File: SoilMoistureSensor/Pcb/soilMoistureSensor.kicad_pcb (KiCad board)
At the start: 2 copper layers, 93 parts, among them J1 USB_B_Micro, J2 Conn_01x03, J3 Conn_01x02, J4 Conn_01x03, J5 Conn_01x03, J6 Conn_01x01, J7 Conn_01x01, J8 Conn_01x01, J9 Conn_01x01, U1 W25Q16JVUXIQ, U10 74AUC2G66, U11 TLV9002S, U12 MCP4011-xxxxMS, U2 RP2040, U3 AP63357Q, U4 74AUC2G86, U5 MIC5504-2.5YM5, U6 74AUC2G86, U7 74AUC2G08, U8 OPA2356xxDGK, U9 74AUC2G66, Y1 12Mhz

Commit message: wip
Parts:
- added R29: 4.3k, Resistor_SMD:R_0603_1608Metric, F.Cu at (189.9, 138.4)
- added R30: 10k, Resistor_SMD:R_0603_1608Metric, F.Cu at (185.9, 138.6)
- C24, C25, C27, C35, C36, C37, C38, R13, R24, R25, R26, R27, R28, U11, U12, U4, U6: moved to B.Cu
- moved J8 88.3 mm to (203.9, 126.4)
- moved J9 88.3 mm to (203.9, 122.3)
- moved J1 69.2 mm to (228.3, 98.7), turned to 180 degrees
- moved J4 67.1 mm to (234.3, 97.7)
- moved J3 63.7 mm to (229.2, 105.8), turned to 90 degrees
- moved U2 60.8 mm to (223.7, 105.6), turned to -90 degrees
- moved J2 60.7 mm to (217.5, 102.3)
- moved D1 57.3 mm to (231.5, 102.7), turned to 90 degrees
- moved J5 54.9 mm to (217.6, 97.7)
- moved R2 50.6 mm to (228.6, 103.0), turned to -90 degrees
- moved R3 45.3 mm to (229.8, 103.0), turned to -90 degrees
- moved C27 10.6 mm to (188.6, 128.5), turned to -90 degrees
- moved C25 10.2 mm to (183.2, 131.4), turned to 0 degrees
- moved C22 10.1 mm to (173.6, 111.6)
- moved U5 10.1 mm to (176.3, 112.3)
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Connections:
- R22 pad 1: Net-(U10-Pad1) -> Net-(U10-Pad2)
- U10 pad 5: Net-(U10-Pad2) -> Net-(R23-Pad1)
- U10 pad 6: Net-(R23-Pad1) -> Net-(U10-Pad1)
- U2 pad 32: /Sens_Clk -> Net-(U2-Pad32)
- U8 pad 6: Net-(U10-Pad2) -> Net-(U10-Pad1)
- U8 pad 7: Net-(U10-Pad2) -> Net-(U10-Pad1)
- U9 pad 1: Net-(R21-Pad1) -> Net-(U8-Pad1)
- U9 pad 2: Net-(U8-Pad1) -> Net-(R21-Pad1)
- U9 pad 5: Net-(U8-Pad1) -> Net-(R20-Pad1)
- U9 pad 6: Net-(R20-Pad1) -> Net-(U8-Pad1)
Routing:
- net Net-(C24-Pad1): track 0.00 -> 8.46 mm
- net Net-(U8-Pad1): track 0.00 -> 7.21 mm
- net Net-(R20-Pad1): track 0.00 -> 7.19 mm
- net +2V5: track 0.00 -> 5.08 mm
- net Net-(R25-Pad1): track 0.00 -> 3.11 mm
- net Net-(R24-Pad1): track 0.00 -> 3.07 mm
- net Net-(R21-Pad1): track 0.00 -> 2.24 mm
- net Net-(J8-Pad1): track 0.00 -> 1.99 mm
- net Net-(R13-Pad2): track 0.00 -> 1.74 mm
- net GND: track 0.00 -> 1.38 mm
- net /Csens: track 0.00 -> 1.15 mm
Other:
- copper layers 2 -> 4
- rule pad_to_mask_clearance: 0 -> 0.05

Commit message: wip
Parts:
- added R31: 20R, Resistor_SMD:R_0603_1608Metric, B.Cu at (233.6, 43.3)
- added R32: 20R, Resistor_SMD:R_0603_1608Metric, B.Cu at (233.6, 44.5)
- C1, C10, C11, C12, C13, C14, C15, C16, C18, C2, C20, C21, C22, C23, C26, C28, C29, C3, C30, C31, C32, C33, C34, C4, C6, C8, C9, D1, J3, J4, J5, L1, L3, R1, R10, R11, R12, R14, R15, R16, R17, R18, R19, R20, R21, R22, R23, R4, R6, R7, U1, U10, U5, U7, U8, U9, Y1: moved to B.Cu
- C24, C25, C27, C35, C36, C37, C38, R13, R24, R25, R26, R27, R28, U11, U12, U4, U6: moved to F.Cu
- J8, J9: footprint TestPoint:TestPoint_Pad_D2.0mm -> TestPoint:TestPoint_Pad_D1.5mm; moved to B.Cu
- moved J7 97.3 mm to (233.8, 84.0)
- moved R30 86.7 mm to (225.2, 61.3), turned to 180 degrees
- moved R14 86.2 mm to (232.1, 61.6)
- moved R29 85.9 mm to (225.2, 60.1)
- moved C25 85.4 mm to (231.4, 61.0), turned to 180 degrees
- moved U4 85.4 mm to (231.4, 58.2)
- moved U7 85.4 mm to (231.4, 58.2)
- moved C28 84.7 mm to (230.9, 61.6)
- moved C23 83.5 mm to (229.7, 58.3)
- moved C24 83.4 mm to (229.6, 57.7)
- moved R13 82.3 mm to (228.6, 55.4), turned to 180 degrees
- moved C22 81.8 mm to (234.0, 56.4), turned to 0 degrees
- moved U9 81.6 mm to (227.9, 58.0)
- moved U6 81.5 mm to (227.8, 58.1)
- moved R20 80.3 mm to (229.0, 55.3), turned to 180 degrees
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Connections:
- D1 pad 2: VBUS -> Net-(D1-Pad2)
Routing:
- net Net-(R20-Pad1): track 7.19 -> 4.71 mm
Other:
- board outline added: 21.3 x 83 mm

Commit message: wip
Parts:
- C4, L1: moved to F.Cu
- moved J7 19.4 mm to (233.0, 64.6)
- moved J6 16.6 mm to (217.6, 68.2)
- moved J8 2.96 mm to (218.7, 53.3)
- moved C4 2.18 mm to (227.3, 53.8)
- moved C13 1.80 mm to (234.1, 51.4)
- moved R11 1.80 mm to (235.2, 51.4)
- moved L3 1.66 mm to (233.2, 54.4)
- moved L1 1.53 mm to (227.9, 51.9), turned to 90 degrees
- moved C28 1.28 mm to (229.9, 62.4), turned to 180 degrees
- moved C9 1.15 mm to (219.0, 51.2), turned to 0 degrees
- moved C18 1.10 mm to (225.3, 53.0)
- moved R1 1.00 mm to (219.2, 49.3)
- moved C1 0.70 mm to (221.0, 46.5)
- moved R22 0.65 mm to (219.5, 54.8)
- moved R23 0.65 mm to (219.5, 56.0)
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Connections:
- R6 pad 2: Net-(R6-Pad2) -> Net-(U2-Pad4)
- R7 pad 1: Net-(R6-Pad2) -> Net-(U2-Pad4)
- U2 pad 11: /GAIN_U/ND -> unconnected-(U2-Pad11)
- U2 pad 12: /GAIN_NCS -> unconnected-(U2-Pad12)
- U2 pad 13: /EN_Sens -> unconnected-(U2-Pad13)
- U2 pad 17: Net-(R6-Pad2) -> unconnected-(U2-Pad17)
- U2 pad 27: unconnected-(U2-Pad27) -> /GAIN_U/ND
- U2 pad 28: unconnected-(U2-Pad28) -> /GAIN_NCS
- U2 pad 37: unconnected-(U2-Pad37) -> /EN_Sens
- U2 pad 4: unconnected-(U2-Pad4) -> Net-(U2-Pad4)
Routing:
- net GND: track 1.38 -> 107.0 mm, vias 0 -> 32
- net +3V3: track 0.00 -> 42.2 mm, vias 0 -> 15
- net /capSens/TRI1: track 0.00 -> 32.6 mm, vias 0 -> 2
- net +2V5: track 5.08 -> 33.1 mm, vias 0 -> 10
- net /capSens/TRI2: track 0.00 -> 22.2 mm, vias 0 -> 3
- net Net-(R15-Pad2): track 0.00 -> 21.7 mm, vias 0 -> 2
- net /EN_Sens: track 0.00 -> 16.4 mm, vias 0 -> 1
- net +1V1: track 0.00 -> 15.7 mm, vias 0 -> 3
- net Net-(U2-Pad4): track 0.00 -> 12.7 mm, vias 0 -> 1
- net Net-(C35-Pad1): track 0.00 -> 12.3 mm, vias 0 -> 1
- net Net-(R29-Pad1): track 0.00 -> 11.5 mm
- net +24V: track 0.00 -> 11.1 mm, vias 0 -> 5
- net /Csens: track 1.15 -> 11.1 mm, vias 0 -> 2
- net Net-(R24-Pad1): track 3.07 -> 11.3 mm
- net Net-(C36-Pad1): track 0.00 -> 7.92 mm, vias 0 -> 1
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- added copper zone on In2.Cu, net +24V
- added copper zone on In2.Cu, net +2V5
- added copper zone on In2.Cu, net +3V3
- added copper zone on In1.Cu, net GND

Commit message: wip
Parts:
- added L4: 1µ, Inductor_SMD:L_0805_2012Metric, F.Cu at (231.9, 47.6)
- moved D1 4.60 mm to (232.0, 42.1), turned to -90 degrees
- moved R2 1.99 mm to (229.7, 44.2)
- moved R3 1.51 mm to (230.8, 44.7)
- moved R8 0.61 mm to (225.3, 43.4)
- moved R32 0.58 mm to (234.2, 44.5)
- moved R6 0.58 mm to (234.2, 42.1)
- moved R7 0.58 mm to (234.2, 40.9)
- moved R31 0.57 mm to (234.1, 43.3)
- moved J1 0.20 mm to (233.8, 42.9)
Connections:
- C5 pad 2: +24V -> Net-(C5-Pad2)
- U3 pad 1: +24V -> Net-(C5-Pad2)
- U3 pad 2: +24V -> Net-(C5-Pad2)
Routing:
- net +24V: track 11.1 -> 5.83 mm, vias 5 -> 4
- net Net-(C5-Pad2): track 0.00 -> 4.81 mm
- net Net-(J4-Pad3): track 3.82 -> 8.02 mm
- net Net-(R2-Pad2): track 6.69 -> 8.26 mm
- net Net-(D1-Pad2): track 4.20 -> 2.86 mm
- net Net-(J1-Pad2): track 2.88 -> 1.60 mm
- net Net-(R3-Pad2): track 7.60 -> 8.59 mm
- net Net-(J1-Pad3): track 3.65 -> 2.76 mm
- net /UART1: track 3.11 -> 2.26 mm
- net Net-(R6-Pad2): track 12.7 -> 13.3 mm

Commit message: wip
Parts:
- J6, J7: moved to B.Cu
- moved J6 5.53 mm to (218.2, 62.7), turned to 180 degrees
- moved J7 1.96 mm to (233.5, 62.7), turned to 180 degrees
- moved C7 0.30 mm to (229.3, 52.0)
- moved C22 0.20 mm to (234.0, 56.6)
- moved L3 0.20 mm to (233.2, 54.6)
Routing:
- net Net-(C29-Pad1): track 0.00 -> 37.7 mm, vias 0 -> 1
- net Net-(C28-Pad1): track 1.28 -> 38.3 mm, vias 0 -> 1
- net GND: track 106.8 -> 110.3 mm, vias 32 -> 33
- net +3V3: track 42.2 -> 45.2 mm
- net Net-(C22-Pad1): track 3.00 -> 5.81 mm
- net Net-(C7-Pad1): track 5.91 -> 7.55 mm
- net +2V5: track 33.1 -> 34.6 mm
- net VBUS: track 6.66 -> 7.88 mm
- net Net-(D1-Pad2): track 2.86 -> 3.97 mm
- net +24V: track 5.83 -> 5.30 mm
- added copper zone on F.Cu, net +24V
- added copper zone on B.Cu, net +2V5
- added copper zone on F.Cu, net +2V5
- added copper zone on F.Cu, net +3V3
- added copper zone on B.Cu, net GND
- added copper zone on F.Cu, net GND
- added copper zone on In1.Cu, net Net-(C28-Pad1)
- added copper zone on In2.Cu, net Net-(C28-Pad1)
- added copper zone on In1.Cu, net Net-(C29-Pad1)
- added copper zone on In2.Cu, net Net-(C29-Pad1)
- added copper zone on F.Cu, net Net-(C5-Pad2)
- added copper zone on F.Cu, net Net-(C7-Pad1)
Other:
- outline, holes or cut-outs redrawn

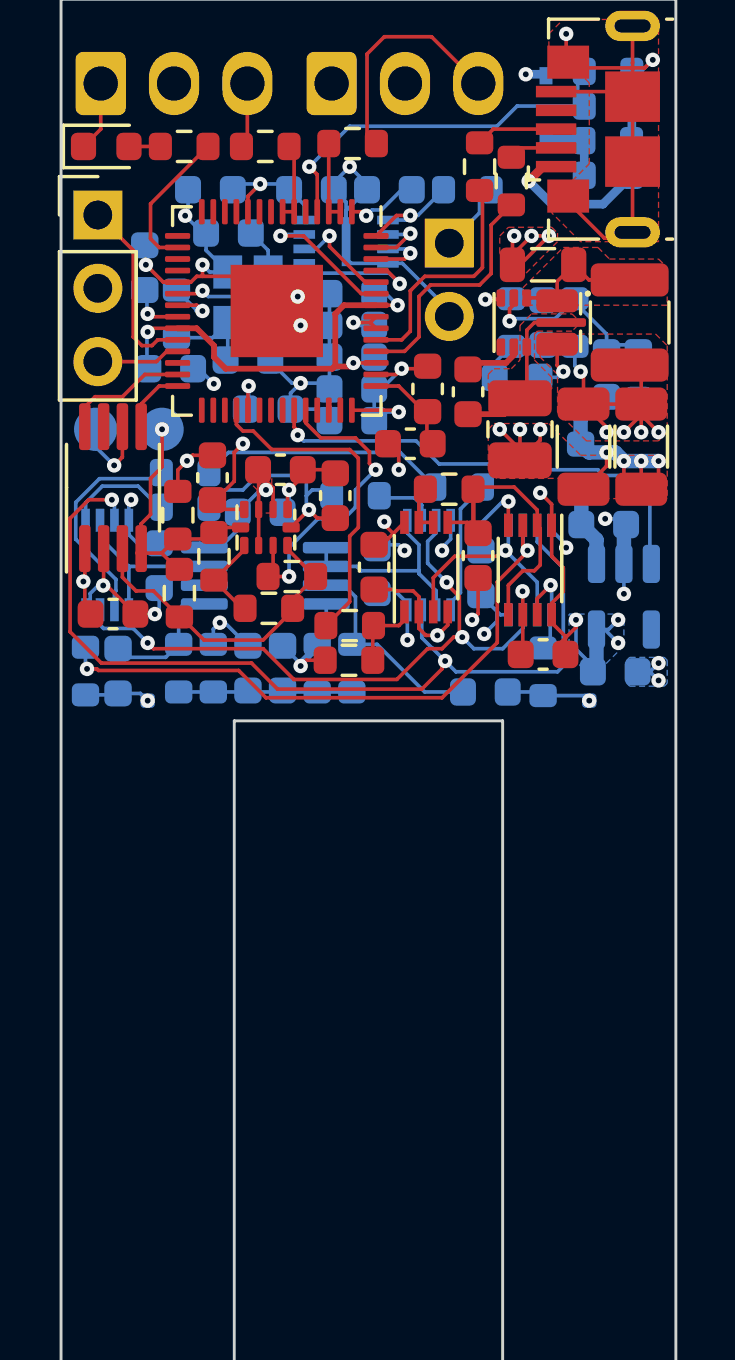
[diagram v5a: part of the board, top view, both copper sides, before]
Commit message: added fluidsensor
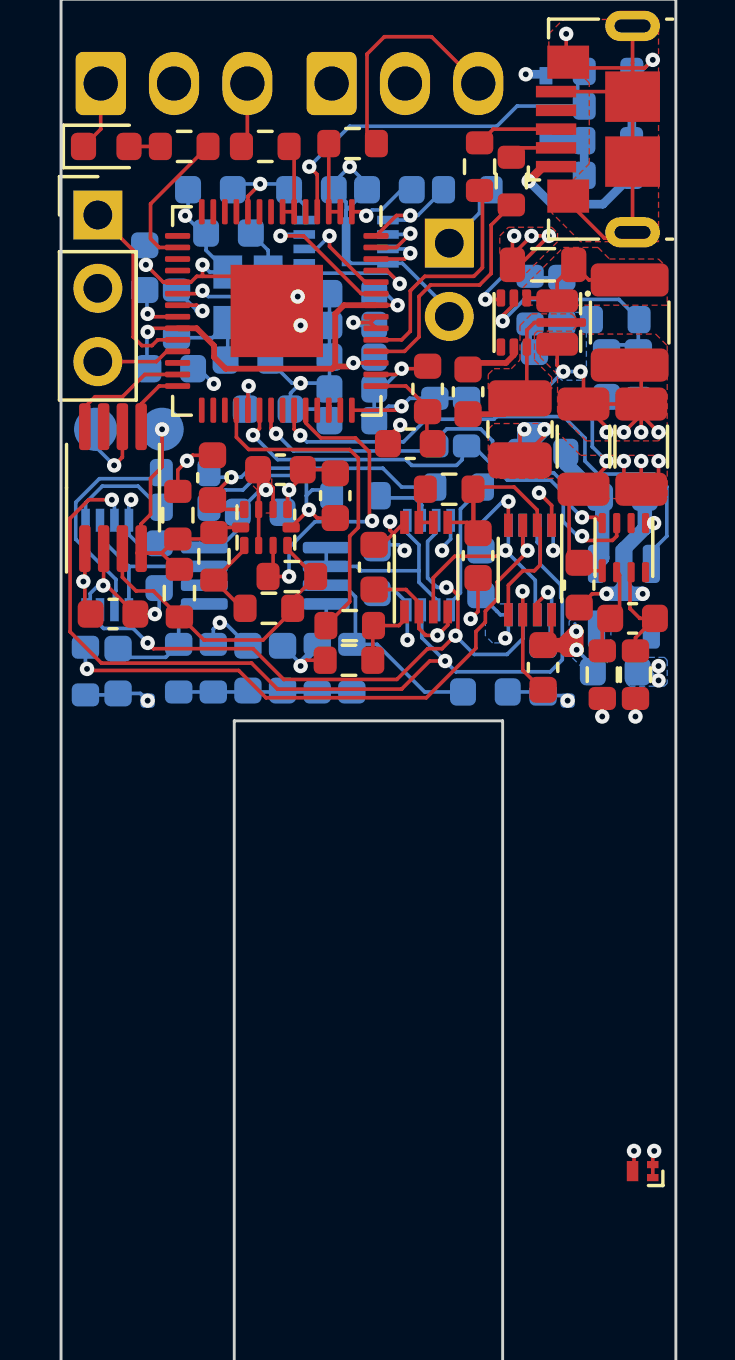
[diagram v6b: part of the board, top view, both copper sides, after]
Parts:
- added C39: 100nF, Capacitor_SMD:C_0603_1608Metric, F.Cu at (233.2, 58.7)
- added C40: 100p, Capacitor_SMD:C_0603_1608Metric, F.Cu at (235.0, 59.9)
- added Q1: MMBZ3904LP, Package_DFN_QFN:Diodes_DFN1006-3, F.Cu at (235.3, 79.0)
- added R33: 10k, Resistor_SMD:R_0603_1608Metric, B.Cu at (229.2, 53.0)
- added R34: 10k, Resistor_SMD:R_0603_1608Metric, B.Cu at (228.2, 53.0)
- added R35: 50R, Resistor_SMD:R_0603_1608Metric, F.Cu at (233.9, 61.8)
- added R36: 50R, Resistor_SMD:R_0603_1608Metric, F.Cu at (235.1, 61.8)
- added U13: TMP451, Bergi:TI_WSON8_2x2mm_noEP, F.Cu at (234.7, 57.4)
- moved R12 1.40 mm to (234.4, 49.5), turned to 180 degrees
- moved L3 1.39 mm to (231.9, 54.1), turned to 0 degrees
- moved C22 1.15 mm to (234.7, 55.6)
- moved C10 1.01 mm to (232.6, 48.8)
- moved R10 1.01 mm to (231.4, 48.8)
- moved J7 0.75 mm to (232.8, 62.7)
- moved C6 0.61 mm to (231.6, 51.4), turned to 90 degrees
- moved C25 0.45 mm to (231.9, 61.5), turned to -90 degrees
- moved R14 0.05 mm to (231.9, 61.6)
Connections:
- U2 pad 34: unconnected-(U2-Pad34) -> /SDA
- U2 pad 35: unconnected-(U2-Pad35) -> /SCL
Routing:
- net Net-(Q1-Pad3): track 0.00 -> 17.2 mm, vias 0 -> 2
- net Net-(Q1-Pad1): track 0.00 -> 16.9 mm, vias 0 -> 2
- net /SDA: track 0.00 -> 16.9 mm, vias 0 -> 2
- net /SCL: track 0.00 -> 14.7 mm, vias 0 -> 2
- net +2V5: track 34.6 -> 30.4 mm, vias 10 -> 9
- net GND: track 110.3 -> 114.1 mm, vias 33 -> 34
- net Net-(U13-Pad3): track 0.00 -> 3.69 mm
- net +3V3: track 45.2 -> 48.6 mm, vias 15 -> 14
- net Net-(U13-Pad2): track 0.00 -> 3.01 mm
- net /EN_Sens: track 16.4 -> 18.5 mm
- net Net-(C35-Pad1): track 12.3 -> 10.4 mm
- net Net-(C13-Pad1): track 6.88 -> 8.49 mm
- net Net-(C22-Pad1): track 5.81 -> 4.47 mm
- net Net-(C10-Pad2): track 2.59 -> 3.68 mm
- net /capSens/TRI2: track 22.2 -> 22.8 mm
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
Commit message: prepare for Manufacturing
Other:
- outline, holes or cut-outs redrawn
- board text added: "SoilMoistureSensor V1.0"
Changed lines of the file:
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@@
     (pad_to_mask_clearance 0.05)
     (solder_mask_min_width 0.1)
+    (aux_axis_origin 215.2 38.4)
+    (grid_origin 215.2 38.4)
     (pcbplotparams
       (layerselection 0x00010fc_ffffffff)
@@
       (net 68 "Net-(J8-Pad1)") (pinfunction "Pin_1") (pintype "passive"))
   )
-  (gr_line (start 221.2 118.4) (end 221.2 63.4) (layer "Edge.Cuts") (width 0.1))
+  (gr_line (start 221.2 118.4) (end 221.2 64.4) (layer "Edge.Cuts") (width 0.1))
   (gr_line (start 236.5 38.4) (end 236.5 118.4) (layer "Edge.Cuts") (width 0.1))
   (gr_line (start 236.5 38.4) (end 215.2 38.4) (layer "Edge.Cuts") (width 0.1))
   (gr_line (start 215.2 38.4) (end 215.2 118.4) (layer "Edge.Cuts") (width 0.1))
   (gr_line (start 233.5 121.4) (end 230.5 118.4) (layer "Edge.Cuts") (width 0.1))
-  (gr_line (start 230.5 63.4) (end 221.2 63.4) (layer "Edge.Cuts") (width 0.1))
+  (gr_line (start 229.5 63.4) (end 222.2 63.4) (layer "Edge.Cuts") (width 0.1))
   (gr_line (start 218.2 121.4) (end 221.2 118.4) (layer "Edge.Cuts") (width 0.1))
   (gr_line (start 236.5 118.4) (end 233.5 121.4) (layer "Edge.Cuts") (width 0.1))
   (gr_line (start 215.2 118.4) (end 218.2 121.4) (layer "Edge.Cuts") (width 0.1))
-  (gr_line (start 230.5 118.4) (end 230.5 63.4) (layer "Edge.Cuts") (width 0.1))
+  (gr_arc (start 229.5 63.4) (mid 230.207107 63.692893) (end 230.5 64.4) (layer "Edge.Cuts") (width 0.1))
+  (gr_arc (start 221.2 64.4) (mid 221.492893 63.692893) (end 222.2 63.4) (layer "Edge.Cuts") (width 0.1))
+  (gr_line (start 230.5 118.4) (end 230.5 64.4) (layer "Edge.Cuts") (width 0.1))
+  (gr_text "SoilMoistureSensor V1.0" (at 218.1 99.3 90) (layer "B.SilkS")
+    (effects (font (size 1 1) (thickness 0.15)) (justify mirror))
+  )
+  (gr_text "SoilMoistureSensor V1.0" (at 218.1 99.2 90) (layer "F.SilkS")
+    (effects (font (size 1 1) (thickness 0.15)))
+  )
   (dimension (type aligned) (layer "Dwgs.User")
     (pts (xy 218.2 121.4) (xy 218.2 38.4))
